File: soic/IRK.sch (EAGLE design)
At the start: 41 parts, among them CON1 FE16-1, IC1 PIC18F25K50, Q1 MMBT2222A, Q2 2N7002, Q3 2N7002, Q4 TSOP4838, Q5 MMBT3906

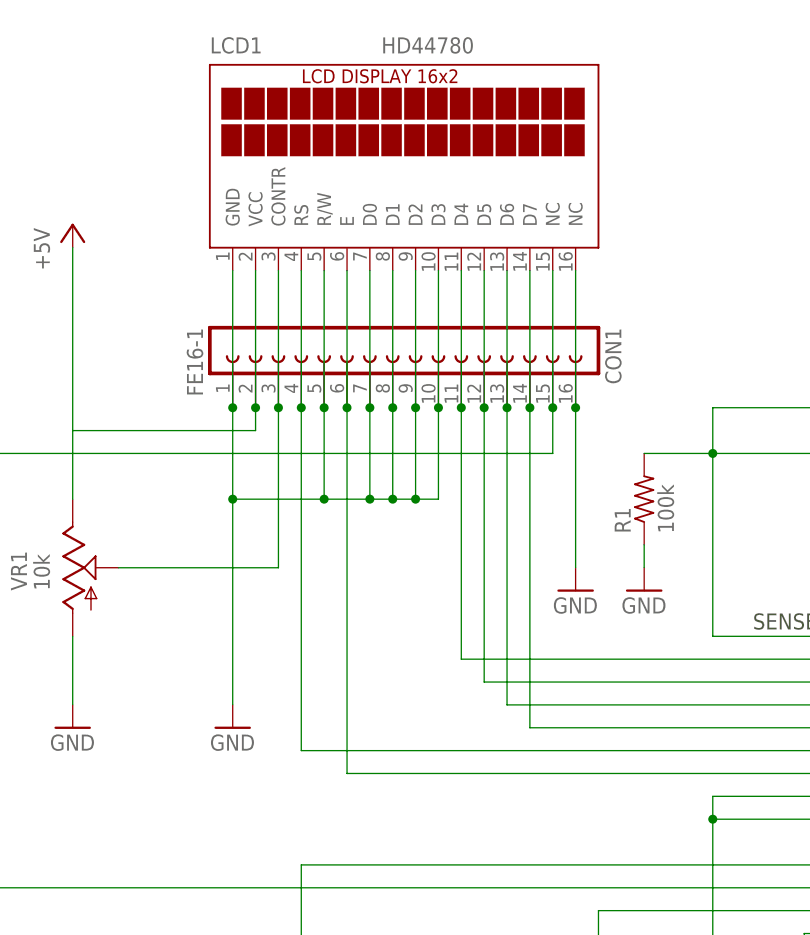
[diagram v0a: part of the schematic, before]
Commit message: Reworked SMD board layout
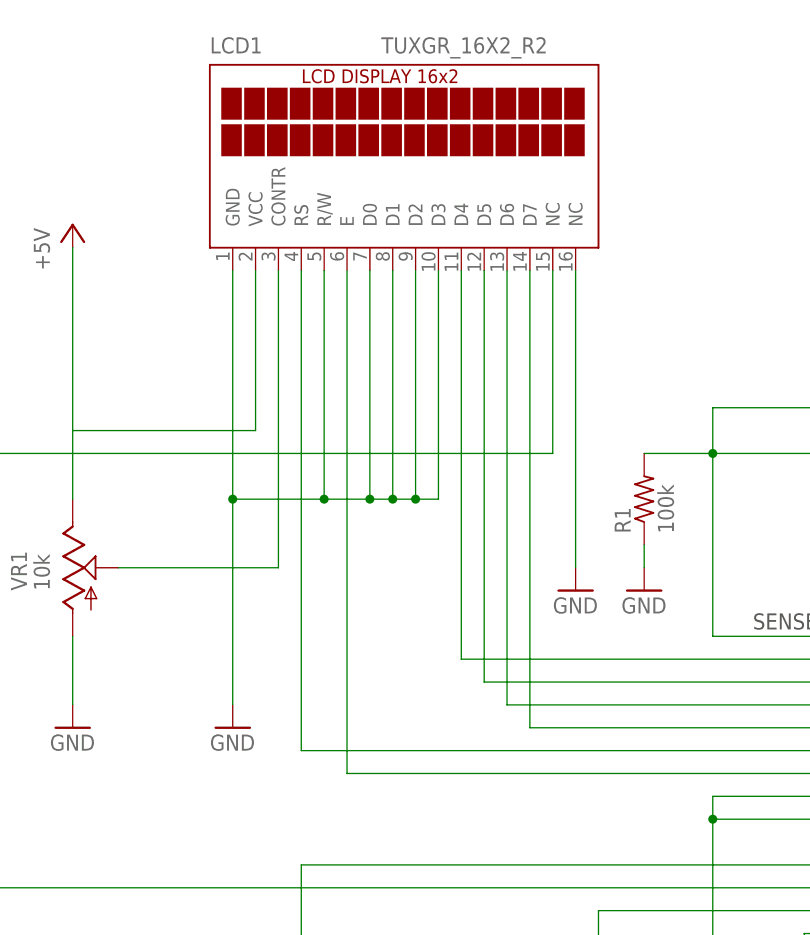
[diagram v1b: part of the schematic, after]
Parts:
- removed CON1: FE16-1, con-lsta-with16:FE16-1
- LCD1: value HD44780 -> TUXGR_16X2_R2; device display-lcd:TUXGR_16X2_R2 -> offboard:TUXGR_16X2_R2
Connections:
- net +5V: no longer CON1.2
- net GND: no longer CON1.1, CON1.10, CON1.16, CON1.5, CON1.7, CON1.8, CON1.9
- net N$1: no longer CON1.11
- net N$2: no longer CON1.12
- net N$3: no longer CON1.13
- net N$31: no longer CON1.15
- net N$4: no longer CON1.14
- net N$5: no longer CON1.4
- net N$6: no longer CON1.6
- net N$7: no longer CON1.3
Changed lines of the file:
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@@
 <parts>
 <part name="IC1" library="microchip" deviceset="PIC18F2*_28" device="W" technology="550" value="PIC18F25K50"/>
-<part name="LCD1" library="display-lcd" deviceset="TUXGR_16X2_R2" device="" value="HD44780"/>
 <part name="P+1" library="supply1" deviceset="+5V" device=""/>
 <part name="P+2" library="supply1" deviceset="+5V" device=""/>
@@
 <part name="GND3" library="supply1" deviceset="GND" device=""/>
 <part name="GND4" library="supply1" deviceset="GND" device=""/>
-<part name="CON1" library="con-lsta-with16" deviceset="FE16-1" device=""/>
 <part name="C2" library="rcl" deviceset="CPOL-EU" device="SMCA" value="4.7uF"/>
 <part name="C1" library="rcl" deviceset="CPOL-EU" device="SMCA" value="4.7uF"/>
@@
 <part name="D1" library="SparkFun-DiscreteSemi" deviceset="DIODE-SCHOTTKY" device="_" value="SS14"/>
 <part name="D3" library="SparkFun-DiscreteSemi" deviceset="DIODE-SCHOTTKY" device="_" value="SS14"/>
+<part name="LCD1" library="offboard" deviceset="TUXGR_16X2_R2" device=""/>
 </parts>
 <sheets>
@@
 <instances>
 <instance part="IC1" gate="G$1" x="78.74" y="48.26"/>
-<instance part="LCD1" gate="G$1" x="-12.7" y="114.3"/>
 <instance part="P+1" gate="1" x="-48.26" y="109.22"/>
 <instance part="P+2" gate="1" x="144.78" y="109.22"/>
@@
 <instance part="GND3" gate="1" x="86.36" y="-15.24"/>
 <instance part="GND4" gate="1" x="101.6" y="-15.24"/>
-<instance part="CON1" gate="G$1" x="-12.7" y="83.82" rot="R270"/>
 <instance part="C2" gate="G$1" x="226.06" y="81.28"/>
 <instance part="C1" gate="G$1" x="175.26" y="40.64"/>
@@
 <instance part="D1" gate="G$1" x="137.16" y="76.2"/>
 <instance part="D3" gate="G$1" x="152.4" y="76.2" rot="R180"/>
+<instance part="LCD1" gate="G$1" x="-12.7" y="114.3"/>
 </instances>
 <busses>
@@
 <segment>
 <wire x1="40.64" y1="60.96" x2="-5.08" y2="60.96" width="0.1524" layer="91"/>
-<wire x1="-5.08" y1="60.96" x2="-5.08" y2="88.9" width="0.1524" layer="91"/>
+<wire x1="-5.08" y1="60.96" x2="-5.08" y2="104.14" width="0.1524" layer="91"/>
 <pinref part="IC1" gate="G$1" pin="RA0/AN0"/>
-<pinref part="CON1" gate="G$1" pin="11"/>
 <pinref part="LCD1" gate="G$1" pin="D4"/>
-<wire x1="-5.08" y1="104.14" x2="-5.08" y2="88.9" width="0.1524" layer="91"/>
-<junction x="-5.08" y="88.9"/>
 </segment>
 </net>
@@
 <segment>
 <wire x1="40.64" y1="58.42" x2="-2.54" y2="58.42" width="0.1524" layer="91"/>
-<wire x1="-2.54" y1="58.42" x2="-2.54" y2="88.9" width="0.1524" layer="91"/>
+<wire x1="-2.54" y1="58.42" x2="-2.54" y2="104.14" width="0.1524" layer="91"/>
 <pinref part="IC1" gate="G$1" pin="RA1/AN1"/>
-<pinref part="CON1" gate="G$1" pin="12"/>
 <pinref part="LCD1" gate="G$1" pin="D5"/>
-<wire x1="-2.54" y1="88.9" x2="-2.54" y2="104.14" width="0.1524" layer="91"/>
-<junction x="-2.54" y="88.9"/>
 </segment>
 </net>
@@
 <segment>
 <wire x1="40.64" y1="55.88" x2="0" y2="55.88" width="0.1524" layer="91"/>
-<wire x1="0" y1="55.88" x2="0" y2="88.9" width="0.1524" layer="91"/>
+<wire x1="0" y1="55.88" x2="0" y2="104.14" width="0.1524" layer="91"/>
 <pinref part="IC1" gate="G$1" pin="RA2/AN2/VREF-/CVREF"/>
-<pinref part="CON1" gate="G$1" pin="13"/>
 <pinref part="LCD1" gate="G$1" pin="D6"/>
-<wire x1="0" y1="104.14" x2="0" y2="88.9" width="0.1524" layer="91"/>
-<junction x="0" y="88.9"/>
 </segment>
 </net>
@@
 <segment>
 <wire x1="40.64" y1="53.34" x2="2.54" y2="53.34" width="0.1524" layer="91"/>
-<wire x1="2.54" y1="53.34" x2="2.54" y2="88.9" width="0.1524" layer="91"/>
+<wire x1="2.54" y1="53.34" x2="2.54" y2="104.14" width="0.1524" layer="91"/>
 <pinref part="IC1" gate="G$1" pin="RA3/AN3/VREF+"/>
-<pinref part="CON1" gate="G$1" pin="14"/>
 <pinref part="LCD1" gate="G$1" pin="D7"/>
-<wire x1="2.54" y1="104.14" x2="2.54" y2="88.9" width="0.1524" layer="91"/>
-<junction x="2.54" y="88.9"/>
 </segment>
 </net>
@@
 <segment>
 <wire x1="40.64" y1="50.8" x2="-22.86" y2="50.8" width="0.1524" layer="91"/>
-<wire x1="-22.86" y1="50.8" x2="-22.86" y2="88.9" width="0.1524" layer="91"/>
+<wire x1="-22.86" y1="50.8" x2="-22.86" y2="104.14" width="0.1524" layer="91"/>
 <pinref part="IC1" gate="G$1" pin="RA4/T0CKI/CIOUT/RCV"/>
-<pinref part="CON1" gate="G$1" pin="4"/>
 <pinref part="LCD1" gate="G$1" pin="RS"/>
-<wire x1="-22.86" y1="104.14" x2="-22.86" y2="88.9" width="0.1524" layer="91"/>
-<junction x="-22.86" y="88.9"/>
 </segment>
 </net>
@@
 <segment>
 <wire x1="40.64" y1="48.26" x2="-17.78" y2="48.26" width="0.1524" layer="91"/>
-<wire x1="-17.78" y1="48.26" x2="-17.78" y2="88.9" width="0.1524" layer="91"/>
+<wire x1="-17.78" y1="48.26" x2="-17.78" y2="104.14" width="0.1524" layer="91"/>
 <pinref part="IC1" gate="G$1" pin="RA5/AN4/!SS!/HLVDIN/C2OUT"/>
-<pinref part="CON1" gate="G$1" pin="6"/>
 <pinref part="LCD1" gate="G$1" pin="E"/>
-<wire x1="-17.78" y1="104.14" x2="-17.78" y2="88.9" width="0.1524" layer="91"/>
-<junction x="-17.78" y="88.9"/>
 </segment>
 </net>
@@
 <wire x1="-48.26" y1="106.68" x2="-48.26" y2="86.36" width="0.1524" layer="91"/>
 <wire x1="-48.26" y1="86.36" x2="-48.26" y2="78.74" width="0.1524" layer="91"/>
-<wire x1="-27.94" y1="88.9" x2="-27.94" y2="86.36" width="0.1524" layer="91"/>
 <wire x1="-27.94" y1="86.36" x2="-48.26" y2="86.36" width="0.1524" layer="91"/>
 <pinref part="P+1" gate="1" pin="+5V"/>
-<pinref part="CON1" gate="G$1" pin="2"/>
 <pinref part="VR1" gate="G$1" pin="E"/>
+<wire x1="-27.94" y1="104.14" x2="-27.94" y2="86.36" width="0.1524" layer="91"/>
 <pinref part="LCD1" gate="G$1" pin="VCC"/>
-<wire x1="-27.94" y1="104.14" x2="-27.94" y2="88.9" width="0.1524" layer="91"/>
-<junction x="-27.94" y="88.9"/>
 </segment>
 <segment>
@@
 <net name="N$7" class="0">
 <segment>
-<wire x1="-25.4" y1="88.9" x2="-25.4" y2="71.12" width="0.1524" layer="91"/>
+<wire x1="-25.4" y1="104.14" x2="-25.4" y2="71.12" width="0.1524" layer="91"/>
 <wire x1="-25.4" y1="71.12" x2="-43.18" y2="71.12" width="0.1524" layer="91"/>
-<pinref part="CON1" gate="G$1" pin="3"/>
 <pinref part="VR1" gate="G$1" pin="S"/>
 <pinref part="LCD1" gate="G$1" pin="CONTR"/>
-<wire x1="-25.4" y1="104.14" x2="-25.4" y2="88.9" width="0.1524" layer="91"/>
-<junction x="-25.4" y="88.9"/>
 </segment>
 </net>
@@
 </segment>
 <segment>
-<wire x1="-30.48" y1="88.9" x2="-30.48" y2="78.74" width="0.1524" layer="91"/>
-<wire x1="-20.32" y1="88.9" x2="-20.32" y2="78.74" width="0.1524" layer="91"/>
 <wire x1="-20.32" y1="78.74" x2="-30.48" y2="78.74" width="0.1524" layer="91"/>
-<wire x1="-15.24" y1="88.9" x2="-15.24" y2="78.74" width="0.1524" layer="91"/>
 <wire x1="-15.24" y1="78.74" x2="-20.32" y2="78.74" width="0.1524" layer="91"/>
-<wire x1="-12.7" y1="88.9" x2="-12.7" y2="78.74" width="0.1524" layer="91"/>
 <wire x1="-12.7" y1="78.74" x2="-15.24" y2="78.74" width="0.1524" layer="91"/>
-<wire x1="-10.16" y1="88.9" x2="-10.16" y2="78.74" width="0.1524" layer="91"/>
 <wire x1="-10.16" y1="78.74" x2="-12.7" y2="78.74" width="0.1524" layer="91"/>
-<wire x1="-7.62" y1="88.9" x2="-7.62" y2="78.74" width="0.1524" layer="91"/>
 <wire x1="-7.62" y1="78.74" x2="-10.16" y2="78.74" width="0.1524" layer="91"/>
 <wire x1="-30.48" y1="55.88" x2="-30.48" y2="78.74" width="0.1524" layer="91"/>
@@
 <junction x="-10.16" y="78.74"/>
 <pinref part="GND25" gate="1" pin="GND"/>
-<pinref part="CON1" gate="G$1" pin="1"/>
-<pinref part="CON1" gate="G$1" pin="5"/>
-<pinref part="CON1" gate="G$1" pin="7"/>
-<pinref part="CON1" gate="G$1" pin="8"/>
-<pinref part="CON1" gate="G$1" pin="9"/>
-<pinref part="CON1" gate="G$1" pin="10"/>
+<wire x1="-30.48" y1="104.14" x2="-30.48" y2="78.74" width="0.1524" layer="91"/>
+<wire x1="-20.32" y1="104.14" x2="-20.32" y2="78.74" width="0.1524" layer="91"/>
+<wire x1="-15.24" y1="104.14" x2="-15.24" y2="78.74" width="0.1524" layer="91"/>
+<wire x1="-12.7" y1="104.14" x2="-12.7" y2="78.74" width="0.1524" layer="91"/>
+<wire x1="-10.16" y1="104.14" x2="-10.16" y2="78.74" width="0.1524" layer="91"/>
+<wire x1="-7.62" y1="104.14" x2="-7.62" y2="78.74" width="0.1524" layer="91"/>
 <pinref part="LCD1" gate="G$1" pin="GND"/>
-<wire x1="-30.48" y1="104.14" x2="-30.48" y2="88.9" width="0.1524" layer="91"/>
-<junction x="-30.48" y="88.9"/>
 <pinref part="LCD1" gate="G$1" pin="R/W"/>
-<wire x1="-20.32" y1="104.14" x2="-20.32" y2="88.9" width="0.1524" layer="91"/>
-<junction x="-20.32" y="88.9"/>
 <pinref part="LCD1" gate="G$1" pin="D0"/>
-<wire x1="-15.24" y1="104.14" x2="-15.24" y2="88.9" width="0.1524" layer="91"/>
-<junction x="-15.24" y="88.9"/>
 <pinref part="LCD1" gate="G$1" pin="D1"/>
-<wire x1="-12.7" y1="104.14" x2="-12.7" y2="88.9" width="0.1524" layer="91"/>
-<junction x="-12.7" y="88.9"/>
 <pinref part="LCD1" gate="G$1" pin="D2"/>
-<wire x1="-10.16" y1="104.14" x2="-10.16" y2="88.9" width="0.1524" layer="91"/>
-<junction x="-10.16" y="88.9"/>
 <pinref part="LCD1" gate="G$1" pin="D3"/>
-<wire x1="-7.62" y1="104.14" x2="-7.62" y2="88.9" width="0.1524" layer="91"/>
-<junction x="-7.62" y="88.9"/>
 </segment>
 <segment>
@@
 </segment>
 <segment>
-<wire x1="7.62" y1="71.12" x2="7.62" y2="88.9" width="0.1524" layer="91"/>
+<wire x1="7.62" y1="71.12" x2="7.62" y2="104.14" width="0.1524" layer="91"/>
 <pinref part="GND6" gate="1" pin="GND"/>
-<pinref part="CON1" gate="G$1" pin="16"/>
 <pinref part="LCD1" gate="G$1" pin="NC@2"/>
-<wire x1="7.62" y1="104.14" x2="7.62" y2="88.9" width="0.1524" layer="91"/>
-<junction x="7.62" y="88.9"/>
 </segment>
 <segment>
@@
 <wire x1="-60.96" y1="83.82" x2="-60.96" y2="91.44" width="0.1524" layer="91"/>
 <wire x1="-60.96" y1="83.82" x2="5.08" y2="83.82" width="0.1524" layer="91"/>
-<wire x1="5.08" y1="83.82" x2="5.08" y2="88.9" width="0.1524" layer="91"/>
-<pinref part="CON1" gate="G$1" pin="15"/>
 <pinref part="Q5" gate="G$1" pin="C"/>
+<wire x1="5.08" y1="104.14" x2="5.08" y2="83.82" width="0.1524" layer="91"/>
 <pinref part="LCD1" gate="G$1" pin="NC@1"/>
-<wire x1="5.08" y1="104.14" x2="5.08" y2="88.9" width="0.1524" layer="91"/>
-<junction x="5.08" y="88.9"/>
-</segment>
-</net>
+</segment>
+</net>
